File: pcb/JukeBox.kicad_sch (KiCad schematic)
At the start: 101 parts, among them J1 USB_C_Receptacle_USB2.0_16P, Q1 Q_NPN_BEC, SW1 SW_SPST, SW10 SW_SPST, SW11 SW_SPST, SW12 SW_SPST, SW2 SW_SPST, SW3 SW_SPST, SW4 SW_SPST, SW5 SW_SPST, SW6 SW_SPST, SW7 SW_SPST, SW8 SW_SPST, SW9 SW_SPST, U1 NCP1117-3.3_SOT223, U2 W25Q128JVS, U3 RP2040, U4 st7789v, U5 CAT24C512, Y2 ABM8-272-T3

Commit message: massive pcb rework for rp2350
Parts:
- removed C10, C8: 1u, Capacitor_SMD:C_0402_1005Metric, symbol Device:C_Small
- removed TP21, TP22, TP23, TP24, TP25, TP26, TP27, TP31, TP32, TP41, TP42, TP51, TP52, TP53, TP54, TP55, TP56: TestPoint, TestPoint:TestPoint_Pad_D1.5mm, symbol Connector:TestPoint
- removed U3: RP2040, JukeBox:RP2040-QFN-56, symbol MCU_RaspberryPi_RP2040:RP2040
- added C10, C6, C7, C8: 4.7u, Capacitor_SMD:C_0402_1005Metric, symbol Device:C
- added C11, C12, C13, C14, C15, C16, C17, C18, C9: 100n, Capacitor_SMD:C_0402_1005Metric, symbol Device:C
- added L1: 3.3u, JukeBox:L_pol_2016, symbol Device:L
- added R15: 33, Resistor_SMD:R_0402_1005Metric, symbol Device:R
- added TP10, TP11: TestPoint, TestPoint:TestPoint_Pad_D1.5mm, symbol Connector:TestPoint
- added U6: RP2350_60QFN, JukeBox:RP2350-QFN-60-1EP_7x7_P0.4mm_EP3.4x3.4mm_ThermalVias, symbol MCU_RaspberryPi_RP2350:RP2350_60QFN
- renumbered C4 to C2, C2 to C4, TP1 to TP12, TP2 to TP13, TP3 to TP14, TP4 to TP15, TP5 to TP16, TP6 to TP17, TP7 to TP18, TP8 to TP19, TP11 to TP21, TP12 to TP22, TP13 to TP23, TP14 to TP24, TP15 to TP25, TP16 to TP26
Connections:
- net +1V1: now also C10.1, C11.1, C7.1, C9.1, L1.1, U6.23 (DVDD), U6.39 (DVDD), U6.50 (VREG_FB), U6.6 (DVDD)
- net +3V3: now also C12.1, C13.1, C14.1, C15.1, C16.1, C17.1, C18.1, C6.1, R15.1, U6.1 (IOVDD), U6.11 (IOVDD), U6.20 (IOVDD), U6.26 (RUN), U6.30 (IOVDD), U6.38 (IOVDD), U6.44 (ADC_AVDD), U6.45 (IOVDD), U6.49 (VREG_VIN), U6.53 (USB_OTP_VDD), U6.54 (QSPI_IOVDD)
- net DBGRX: now also U6.2 (GPIO0)
- net DBGSC: now also U6.24 (SWCLK)
- net DBGSD: now also U6.25 (SWD)
- net DBGTX: now also U6.3 (GPIO1)
- net GND: now also C10.2, C11.2, C12.2, C13.2, C14.2, C15.2, C16.2, C17.2, C18.2, C6.2, C7.2, C8.2, C9.2, U6.47 (VREG_PGND), U6.61 (GND)
- net GPIO26_ADC0: now also U6.40 (GPIO26_ADC0)
- net GPIO27_ADC1: now also U6.41 (GPIO27_ADC1)
- net GPIO28_ADC2: now also U6.42 (GPIO28_ADC2)
- net GPIO3: now also U6.5 (GPIO3)
- net QSPI_SCLK: now also U6.56 (QSPI_SCLK)
- net QSPI_SD0: now also U6.57 (QSPI_SD0)
- net QSPI_SD1: now also U6.59 (QSPI_SD1)
- net QSPI_SD2: now also U6.58 (QSPI_SD2)
- net QSPI_SD3: now also U6.55 (QSPI_SD3)
- net QSPI_SS: now also U6.60 (QSPI_SS)
- net USB_D+: now also TP10.1
- net USB_D-: now also TP11.1
- net USB_R_D+: now also U6.52 (USB_DP)
- net USB_R_D-: now also U6.51 (USB_DM)
- net XIN: now also U6.21 (XIN)
- net XOUT: now also U6.22 (XOUT)
- net GPIO10 renamed KBROW2
- net KBROW2: now also U6.10 (GPIO7)
- net GPIO11 renamed KBROW3
- net KBROW3: now also U6.12 (GPIO8)
- net GPIO12 renamed KBCOL1
- net KBCOL1: now also U6.13 (GPIO9)
- net GPIO13 renamed KBCOL2
- net KBCOL2: now also U6.14 (GPIO10)
- net GPIO14 renamed KBCOL3
- net KBCOL3: now also U6.15 (GPIO11)
- net GPIO15 renamed KBCOL4
- net KBCOL4: now also U6.16 (GPIO12)
- net GPIO16 renamed SCRBL
- net SCRBL: now also U6.27 (GPIO16)
- net GPIO17 renamed SCRRST
- net SCRRST: now also U6.17 (GPIO13)
- net GPIO18 renamed SCRDC
- net SCRDC: now also U6.19 (GPIO15)
- net GPIO19 renamed SCRCS
- net SCRCS: now also U6.18 (GPIO14)
- net GPIO2 renamed RGBDIN
- net RGBDIN: now also U6.4 (GPIO2)
- net GPIO20 renamed SCRCLK
- net SCRCLK: now also U6.28 (GPIO17)
- net GPIO21 renamed SCRDIN
- net GPIO25 renamed LEDPIN
- net LEDPIN: now also U6.43 (GPIO29_ADC3)
- net GPIO4 renamed I2C0SDA
- net I2C0SDA: now also U6.7 (GPIO4)
- net GPIO5 renamed I2C0SCL
- net I2C0SCL: now also U6.8 (GPIO5)
- net GPIO9 renamed KBROW1
- net KBROW1: now also U6.9 (GPIO6)
- new net SCRD0: U6.37 (GPIO25)
- new net SCRD1: U6.36 (GPIO24)
- new net SCRD2: U6.35 (GPIO23)
- new net SCRD3: U6.34 (GPIO22)
- new net SCRD4: U6.33 (GPIO21)
- new net SCRD5: U6.32 (GPIO20)
- new net SCRD6: U6.31 (GPIO19)
- new net SCRD7: U6.29 (GPIO18)
- new net VREG_AVDD: C8.1, R15.2, U6.46 (VREG_AVDD)
- new net VREG_LX: L1.2, U6.48 (VREG_LX)
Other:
- note added: "Make sure R3 and R4 are close to RP2350"
- note removed: "Make sure C8/C10 is close to pin 45/44 of RP2040"
- note removed: "Make sure R3 and R4 are close to RP2040"
- moved on the sheet: C5, H1, H2, H3, H4, JP1, Q1, R1, R13, R14, TP12, TP13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

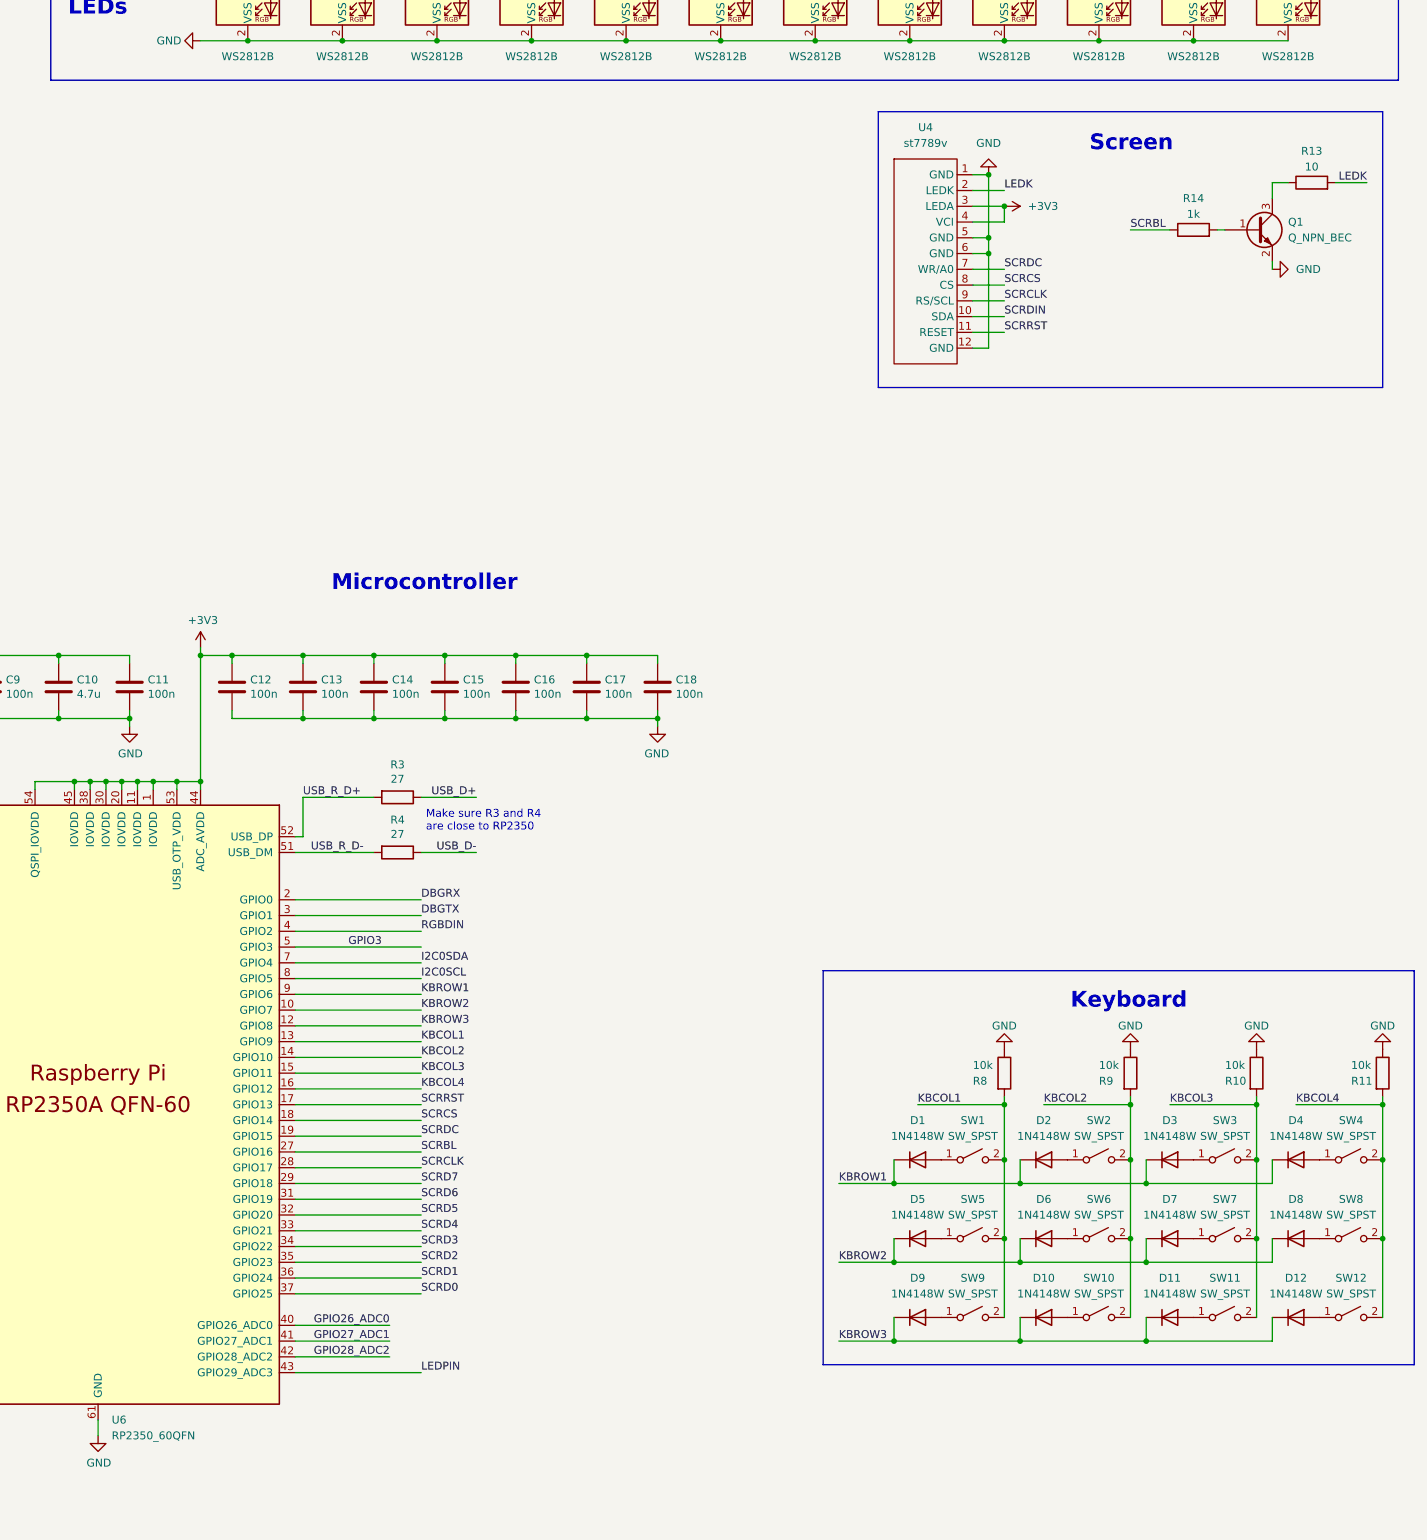
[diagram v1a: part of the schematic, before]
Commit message: add new screen footprint and route traces. update bom
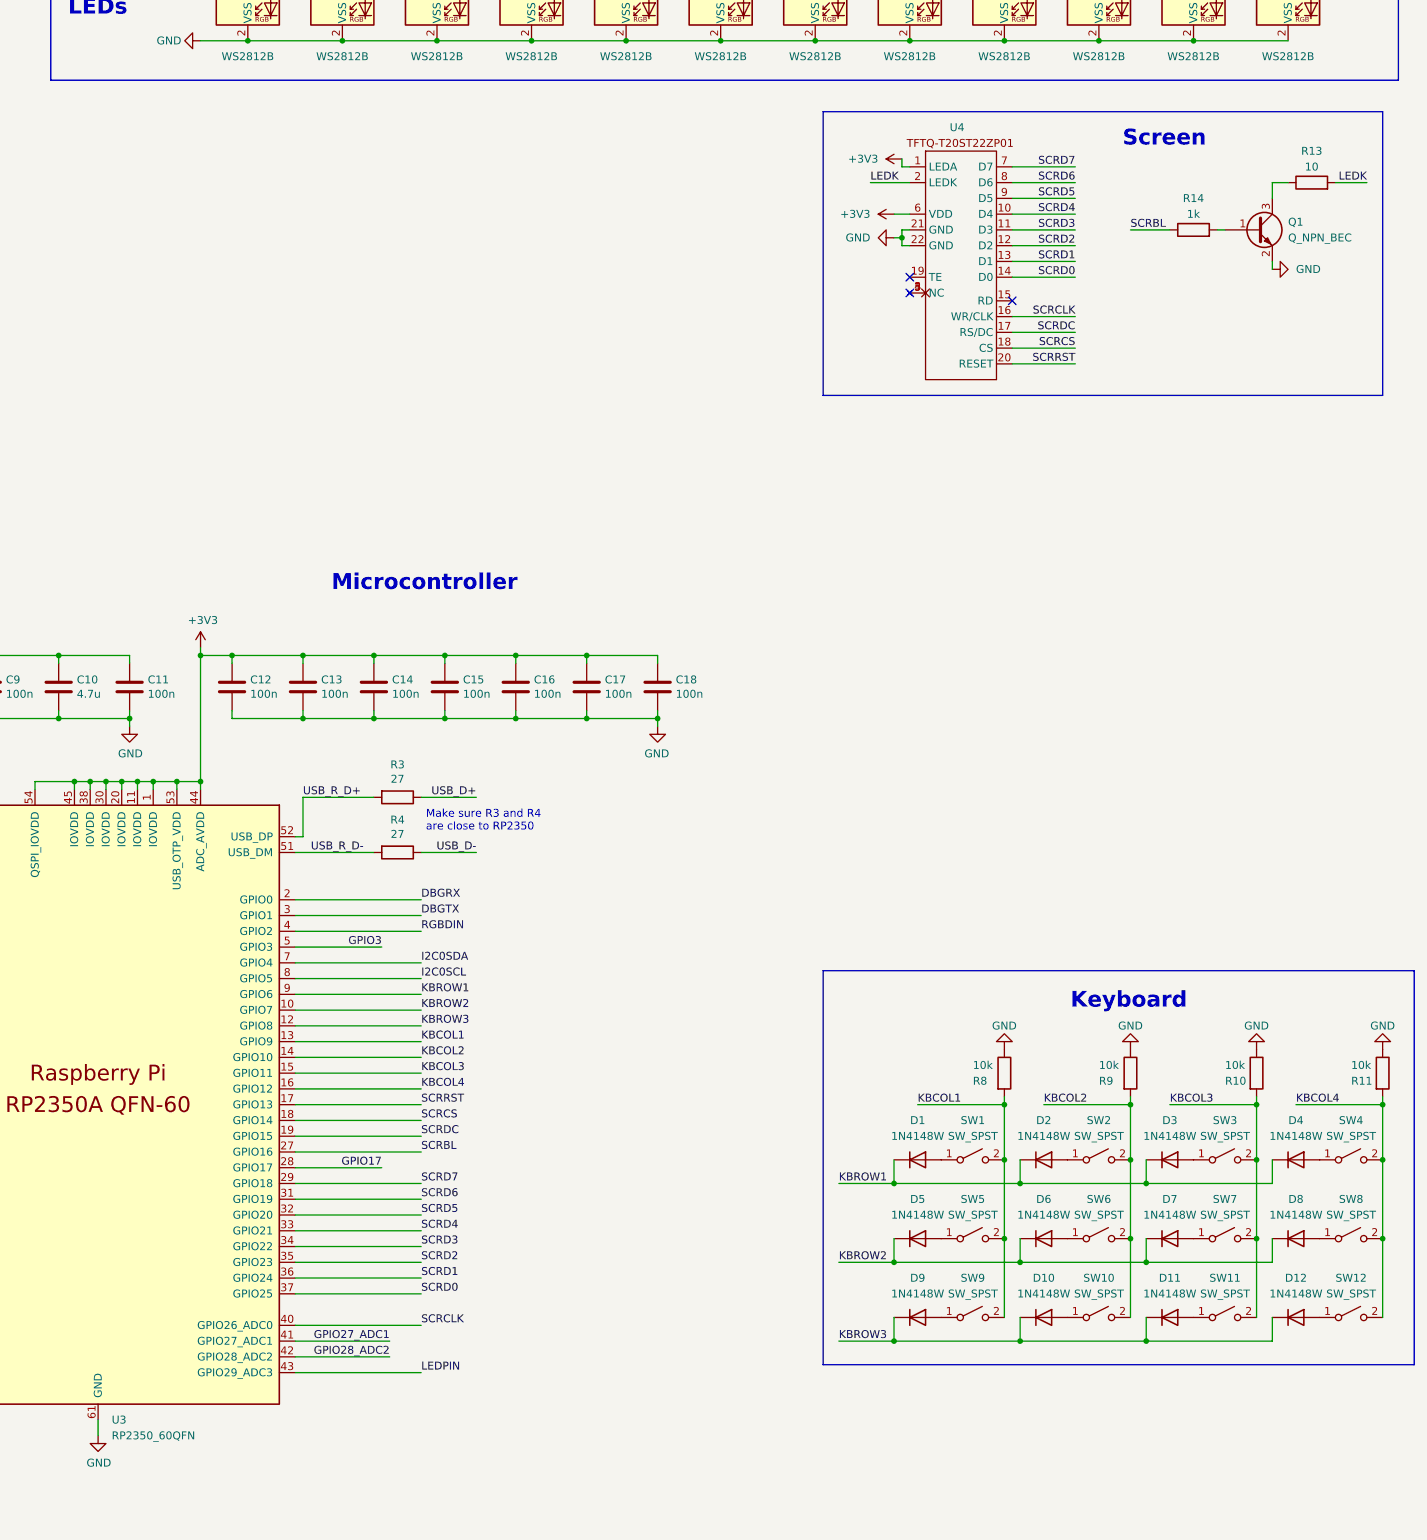
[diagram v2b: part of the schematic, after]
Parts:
- removed U4: st7789v, JukeBox:st7789v, symbol st7789v:st7789v
- added U4: ~, JukeBox:TFTQ-T20ST22ZP01, symbol TFTQ-T20ST22ZP01:TFTQ-T20ST22ZP01
- renumbered U6 to U3
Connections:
- net GPIO26_ADC0 is gone; now on net SCRCLK: U3.40 (GPIO26_ADC0)
- net +3V3: now also U4.1 (LEDA), U4.6 (VDD)
- net GND: now also U4.21 (GND), U4.22 (GND)
- net LEDK: now also U4.2 (LEDK)
- net SCRCLK: now also U4.16 (WR/CLK); no longer U3.28 (GPIO17)
- net SCRCS: now also U4.18 (CS)
- net SCRD0: now also U4.14 (D0)
- net SCRD1: now also U4.13 (D1)
- net SCRD2: now also U4.12 (D2)
- net SCRD3: now also U4.11 (D3)
- net SCRD4: now also U4.10 (D4)
- net SCRD5: now also U4.9 (D5)
- net SCRD6: now also U4.8 (D6)
- net SCRD7: now also U4.7 (D7)
- net SCRDC: now also U4.17 (RS/DC)
- net SCRRST: now also U4.20 (RESET)
- new net: U4.3 (NC), U4.4 (NC), U4.5 (NC)
- new net GPIO17: U3.28 (GPIO17)
- no-connect marks 2 -> 5

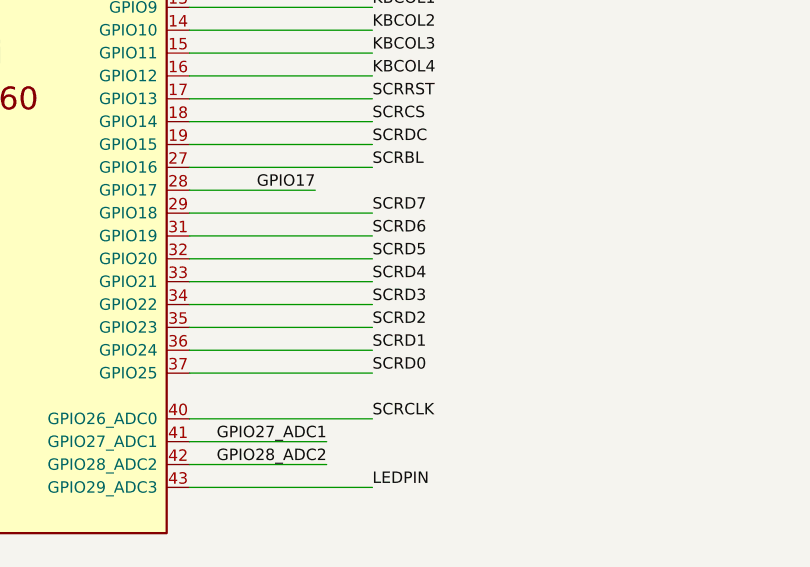
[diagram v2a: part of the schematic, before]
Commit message: reorder screen pins (will make programming later easier)
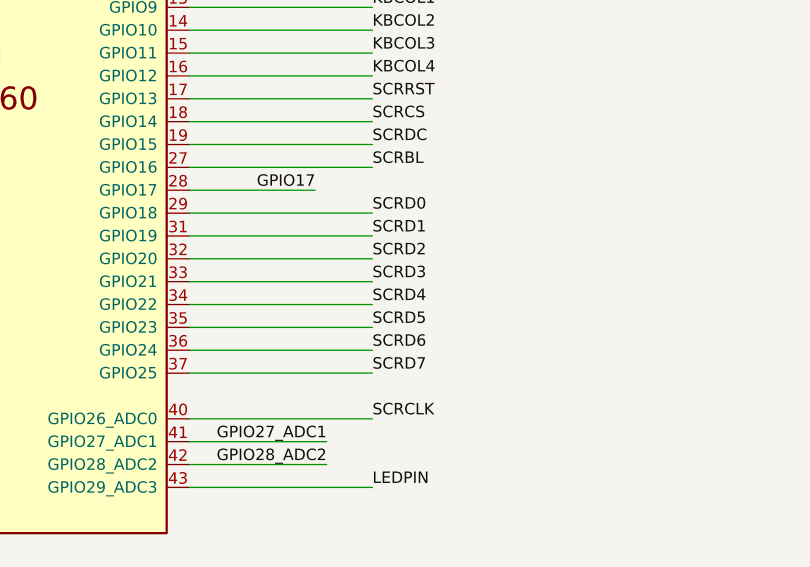
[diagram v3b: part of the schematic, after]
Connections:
- net SCRD0: now also U3.29 (GPIO18); no longer U3.37 (GPIO25)
- net SCRD1: now also U3.31 (GPIO19); no longer U3.36 (GPIO24)
- net SCRD2: now also U3.32 (GPIO20); no longer U3.35 (GPIO23)
- net SCRD3: now also U3.33 (GPIO21); no longer U3.34 (GPIO22)
- net SCRD4: now also U3.34 (GPIO22); no longer U3.33 (GPIO21)
- net SCRD5: now also U3.35 (GPIO23); no longer U3.32 (GPIO20)
- net SCRD6: now also U3.36 (GPIO24); no longer U3.31 (GPIO19)
- net SCRD7: now also U3.37 (GPIO25); no longer U3.29 (GPIO18)
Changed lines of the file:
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@@
 	)
 	(label "SCRD0"
-		(at 246.38 240.03 0)
-		(effects
-			(font
-				(size 1.27 1.27)
-			)
-			(justify left bottom)
-		)
-	)
-	(label "SCRD3"
-		(at 246.38 232.41 0)
+		(at 246.38 222.25 0)
 		(effects
 			(font
@@
 		)
 	)
+	(label "SCRD5"
+		(at 246.38 234.95 0)
+		(effects
+			(font
+				(size 1.27 1.27)
+			)
+			(justify left bottom)
+		)
+	)
 	(label "SCRBL"
 		(at 246.38 217.17 0)
@@
 		)
 	)
+	(label "SCRD6"
+		(at 246.38 237.49 0)
+		(effects
+			(font
+				(size 1.27 1.27)
+			)
+			(justify left bottom)
+		)
+	)
 	(label "USB_D-"
 		(at 86.36 200.66 180)
@@
 		)
 	)
+	(label "SCRD7"
+		(at 246.38 240.03 0)
+		(effects
+			(font
+				(size 1.27 1.27)
+			)
+			(justify left bottom)
+		)
+	)
 	(label "DBGTX"
 		(at 246.38 179.07 0)
@@
 		)
 	)
-	(label "SCRD2"
-		(at 246.38 234.95 0)
-		(effects
-			(font
-				(size 1.27 1.27)
-			)
-			(justify left bottom)
-		)
-	)
 	(label "LEDPIN"
 		(at 172.72 43.18 180)
@@
 		)
 	)
-	(label "SCRD5"
-		(at 246.38 227.33 0)
+	(label "SCRD3"
+		(at 246.38 229.87 0)
 		(effects
 			(font
@@
 		)
 	)
+	(label "SCRD4"
+		(at 246.38 232.41 0)
+		(effects
+			(font
+				(size 1.27 1.27)
+			)
+			(justify left bottom)
+		)
+	)
 	(label "QSPI_SS"
 		(at 35.56 113.03 0)
@@
 		)
 	)
+	(label "SCRD2"
+		(at 246.38 227.33 0)
+		(effects
+			(font
+				(size 1.27 1.27)
+			)
+			(justify left bottom)
+		)
+	)
 	(label "SCRRST"
 		(at 351.79 90.17 180)
@@
 		)
 	)
-	(label "SCRD1"
-		(at 246.38 237.49 0)
-		(effects
-			(font
-				(size 1.27 1.27)
-			)
-			(justify left bottom)
-		)
-	)
 	(label "GPIO17"
 		(at 240.03 219.71 180)
@@
 		)
 	)
-	(label "SCRD6"
-		(at 246.38 224.79 0)
-		(effects
-			(font
-				(size 1.27 1.27)
-			)
-			(justify left bottom)
-		)
-	)
 	(label "QSPI_SD2"
 		(at 151.13 196.85 0)
@@
 		)
 	)
-	(label "SCRD7"
-		(at 246.38 222.25 0)
-		(effects
-			(font
-				(size 1.27 1.27)
-			)
-			(justify left bottom)
-		)
-	)
 	(label "DBGRX"
 		(at 34.29 199.39 180)
@@
 		)
 	)
-	(label "SCRD4"
-		(at 246.38 229.87 0)
-		(effects
-			(font
+	(label "SCRD1"
+		(at 246.38 224.79 0)
+		(effects
+			(font
